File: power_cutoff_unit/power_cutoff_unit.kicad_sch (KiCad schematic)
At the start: 48 parts, among them J1 Conn_01x02, J10 Conn_01x04, J2 Conn_01x02, J3 Conn_01x02, J4 Conn_01x02, J5 Conn_01x02, J6 Conn_01x02, J7 Conn_01x02, J8 Conn_01x02, J9 Conn_01x02_Pin, K2 T9GS1L14-5, Q1 AO3400A, SW1 SW_DIP_x02, U1 ADuM120N, U2 STM32F303K8Tx, U3 ADP3338AKCZ-3.3, U4 MCP2562-E-SN, U6 LMZ14201H

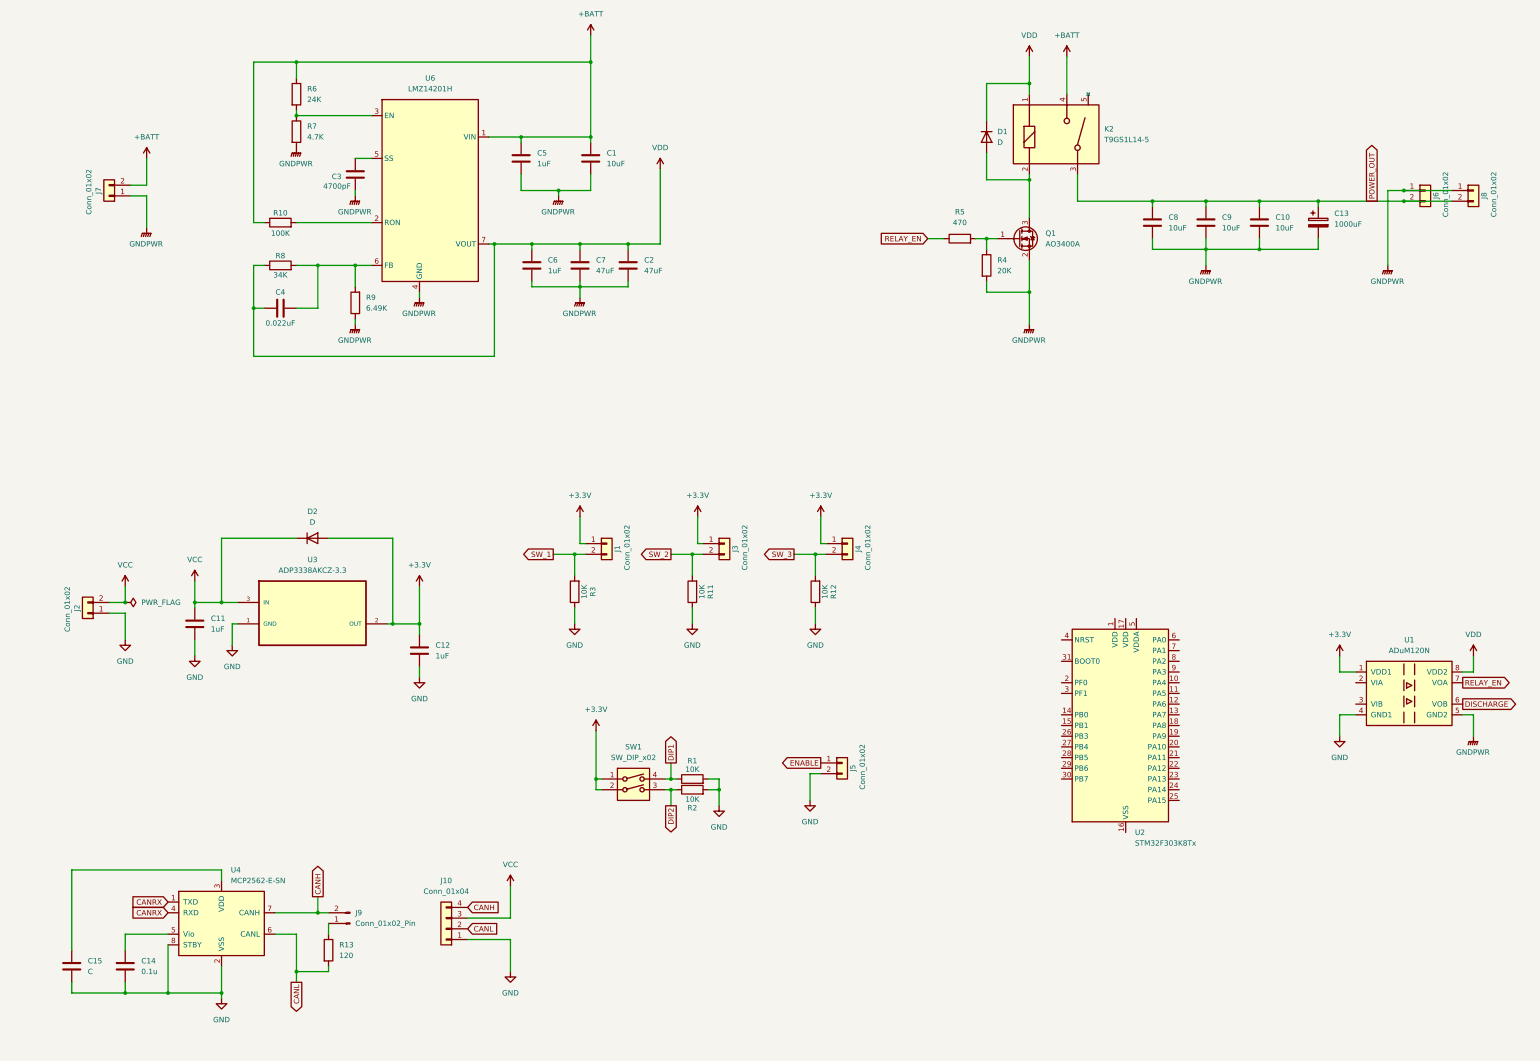
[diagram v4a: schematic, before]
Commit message: 5Vを選択的にした
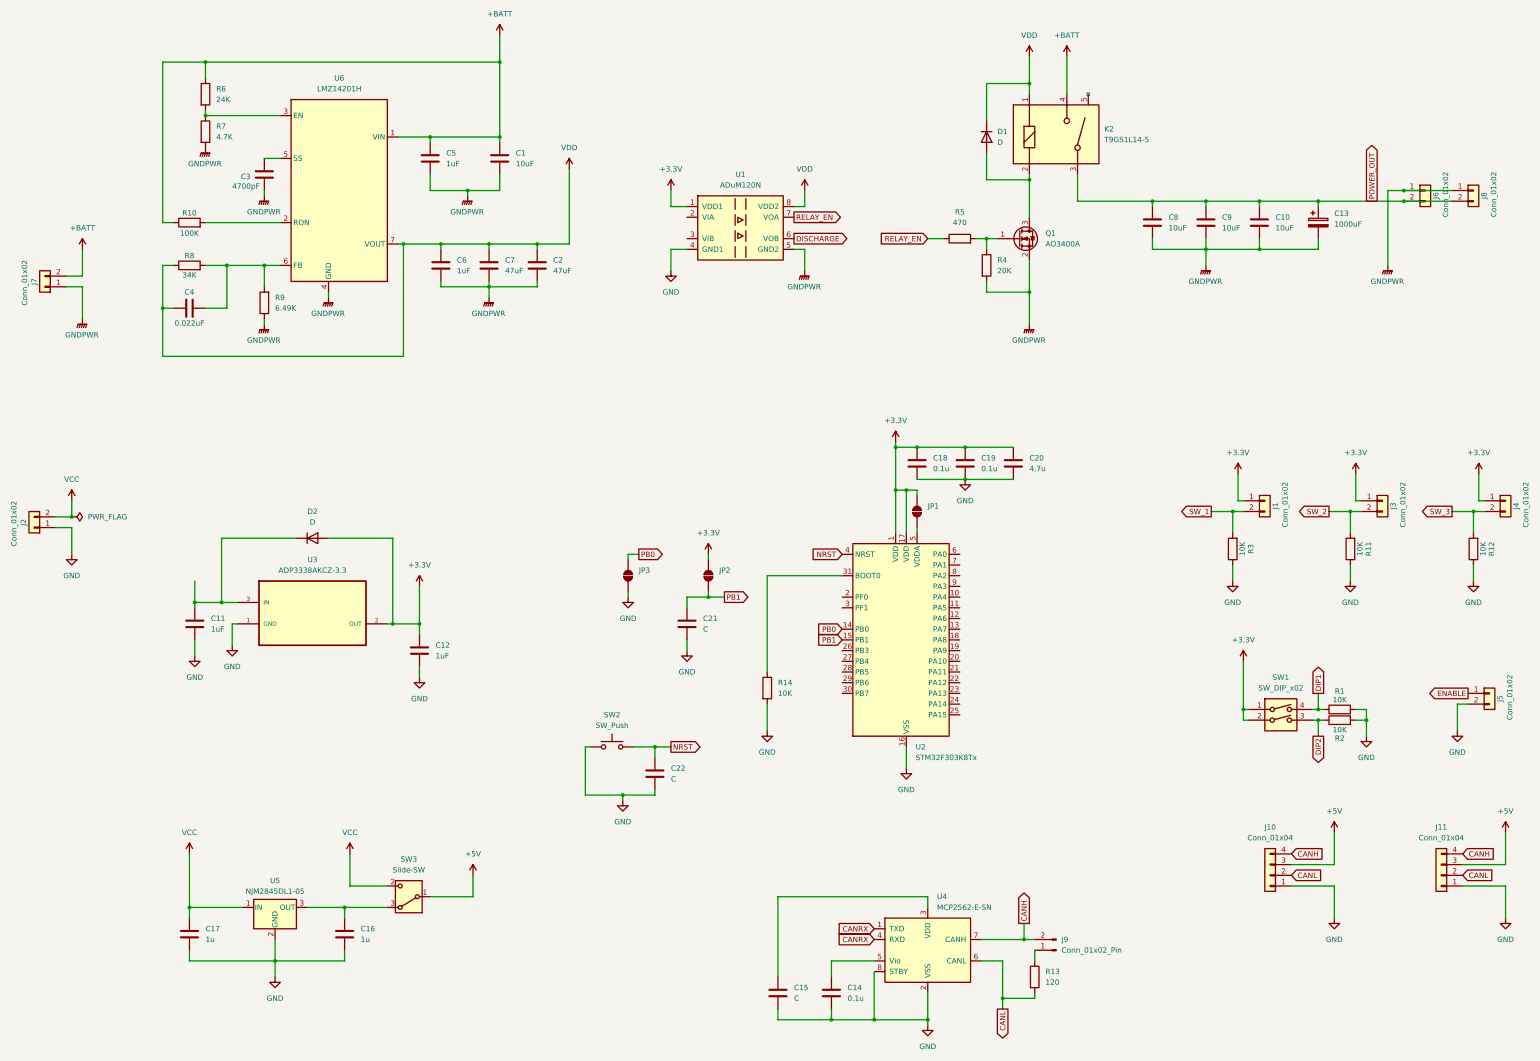
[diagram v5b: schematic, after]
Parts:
- added C16, C17: 1u, symbol Device:C
- added C18, C19: 0.1u, symbol Device:C
- added C20: 4.7u, symbol Device:C
- added C21, C22: C, symbol Device:C
- added J11: Conn_01x04, symbol Connector_Generic:Conn_01x04
- added JP1, JP2, JP3: SolderJumper_2_Open, symbol Jumper:SolderJumper_2_Open
- added R14: 10K, symbol Device:R
- added SW2: SW_Push, symbol Switch:SW_Push
- added SW3: Slide-SW, Button_Switch_THT:SW_Slide-03_Wuerth-WS-SLTV_10x2.5x6.4_P2.54mm, symbol Switch:SW_Wuerth_450301014042
- added U5: NJM2845DL1-05, Package_TO_SOT_SMD:TO-252-3_TabPin2, symbol Regulator_Linear:L7805
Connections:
- net +3.3V: now also U2.1 (VDD), U2.17 (VDD), C18.1, C19.1, C20.1, JP1.2 (B), JP2.2 (B)
- net CANH: now also J11.4 (Pin_4)
- net CANL: now also J11.2 (Pin_2)
- net GND: now also U2.16 (VSS), U2.32 (VSS), C16.2, C17.2, C18.2, C19.2, C20.2, C21.2, C22.2, J11.1 (Pin_1), JP3.1 (A), R14.2, SW2.1, U5.2 (GND)
- net VCC: now also C17.1, SW3.2 (C), U5.1 (IN); no longer C11.1, D2.1 (K), J10.3 (Pin_3), U3.3 (IN)
- net PB0: now reaches U2.14 (PB0)
- net PB0: now also JP3.2 (B)
- net PB1: now reaches U2.15 (PB1)
- net PB1: now also C21.1, JP2.1 (A)
- net at U2.31 (BOOT0): now also R14.1
- net NRST: now reaches U2.4 (NRST)
- net NRST: now also C22.1, SW2.2
- net at U2.5 (VDDA): now also JP1.1 (A)
- new net: C16.1, SW3.3 (A), U5.3 (OUT)
- new net: C11.1, D2.1 (K), U3.3 (IN)
- new net +5V: J10.3 (Pin_3), J11.3 (Pin_3), SW3.1 (B)
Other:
- moved on the sheet: C1, C14, C15, C2, C3, C4, C5, C6, C7, J1, J10, J2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

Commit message: CubeMXでプロジェクト作成
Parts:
- removed C8: 10uF, symbol Device:C
- added C23: 1000uF, Capacitor_THT:CP_Radial_D16.0mm_P7.50mm, symbol Device:C_Polarized
- added D3: LED, symbol Device:LED
- added Q2: SSM3K341R, Package_TO_SOT_SMD:SOT-23_Handsoldering, symbol Device:Q_NMOS_GDS
- added R15: 25, Package_TO_SOT_THT:TO-220-2_Vertical, symbol Device:R
- added R16, R18: 1K, symbol Device:R
- added R17: 20K, symbol Device:R
- C13: footprint (none) -> Capacitor_THT:CP_Radial_D16.0mm_P7.50mm
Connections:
- net +5V: now also C11.1, D2.1 (K), U3.3 (IN)
- net DISCHARGE: now also R18.1
- net GNDPWR: now also C23.2, Q2.3 (S), R17.2
- net POWER_OUT: now also C23.1, R15.1, R16.1
- new net: Q2.1 (G), R17.1, R18.2
- new net: D3.1 (K), Q2.2 (D), R15.2
- new net: D3.2 (A), R16.2
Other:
- company: (none) -> TMCIT-Arakawa
- title: (none) -> GN10PowerCutoffUnit
- moved on the sheet: C1, C10, C11, C12, C13, C14, C15, C16, C17, C18, C19, C2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

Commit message: MOSFET修正とCの値入れた。
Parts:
- removed Q1: AO3400A, Package_TO_SOT_SMD:SOT-23, symbol Transistor_FET:AO3400A
- removed Q2: SSM3K341R, Package_TO_SOT_SMD:SOT-23_Handsoldering, symbol Device:Q_NMOS_GDS
- added Q1, Q2: SSM3K341R, Package_TO_SOT_SMD:SOT-23_Handsoldering, symbol Device:Q_NMOS_GSD
- C13, C23: value 1000uF -> 1000u
- C15, C21, C22: value C -> 0.1u
- D1: value D -> SS2040FL; footprint (none) -> Diode_SMD:D_SOD-123F
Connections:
- net GNDPWR: now also Q1.2 (S), Q2.2 (S)
- net at D1.2 (A), K2.2: now also Q1.3 (D)
- net at R4.1, R5.2: now also Q1.1 (G)
- net at R17.1, R18.2: now also Q2.1 (G)
- net at D3.1 (K), R15.2: now also Q2.3 (D)
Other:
- moved on the sheet: D1
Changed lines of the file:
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@@
 	(wire
 		(pts
-			(xy 201.93 46.99) (xy 201.93 38.1)
+			(xy 194.31 46.99) (xy 194.31 38.1)
 		)
 		(stroke
@@
 	(wire
 		(pts
-			(xy 201.93 60.96) (xy 212.09 60.96)
+			(xy 194.31 60.96) (xy 212.09 60.96)
 		)
 		(stroke
@@
 	(wire
 		(pts
-			(xy 201.93 54.61) (xy 201.93 60.96)
+			(xy 194.31 54.61) (xy 194.31 60.96)
 		)
 		(stroke
@@
 	(wire
 		(pts
-			(xy 201.93 38.1) (xy 212.09 38.1)
+			(xy 194.31 38.1) (xy 212.09 38.1)
 		)
 		(stroke
@@
 	(symbol
 		(lib_id "Device:D")
-		(at 201.93 50.8 270)
+		(at 194.31 50.8 270)
 		(unit 1)
 		(exclude_from_sim no)
@@
 		(fields_autoplaced yes)
 		(property "Reference" "D1"
-			(at 204.47 49.5299 90)
+			(at 196.85 49.5299 90)
 			(effects
 				(font
@@
 			)
 		)
-		(property "Value" "D"
-			(at 204.47 52.0699 90)
+		(property "Value" "SS2040FL"
+			(at 196.85 52.0699 90)
 			(effects
 				(font
@@
 			)
 		)
-		(property "Footprint" ""
-			(at 201.93 50.8 0)
+		(property "Footprint" "Diode_SMD:D_SOD-123F"
+			(at 194.31 50.8 0)
 			(effects
 				(font
@@
 		)
 		(property "Datasheet" "~"
-			(at 201.93 50.8 0)
+			(at 194.31 50.8 0)
 			(effects
 				(font
@@
 		)
 		(property "Description" "Diode"
-			(at 201.93 50.8 0)
+			(at 194.31 50.8 0)
 			(effects
 				(font
@@
 		)
 		(property "Sim.Device" "D"
-			(at 201.93 50.8 0)
+			(at 194.31 50.8 0)
 			(effects
 				(font
@@
 		)
 		(property "Sim.Pins" "1=K 2=A"
-			(at 201.93 50.8 0)
+			(at 194.31 50.8 0)
 			(effects
 				(font
@@
 			)
 		)
-		(property "Value" "C"
+		(property "Value" "0.1u"
 			(at 142.24 264.1599 0)
 			(effects
@@
 	)
 	(symbol
-		(lib_id "Transistor_FET:AO3400A")
-		(at 209.55 74.93 0)
-		(unit 1)
-		(exclude_from_sim no)
-		(in_bom yes)
-		(on_board yes)
-		(dnp no)
-		(fields_autoplaced yes)
-		(property "Reference" "Q1"
-			(at 215.9 73.6599 0)
-			(effects
-				(font
-					(size 1.27 1.27)
-				)
-				(justify left)
-			)
-		)
-		(property "Value" "AO3400A"
-			(at 215.9 76.1999 0)
-			(effects
-				(font
-					(size 1.27 1.27)
-				)
-				(justify left)
-			)
-		)
-		(property "Footprint" "Package_TO_SOT_SMD:SOT-23"
-			(at 214.63 76.835 0)
-			(effects
-				(font
-					(size 1.27 1.27)
-					(italic yes)
-				)
-				(justify left)
-				(hide yes)
-			)
-		)
-		(property "Datasheet" "http://www.aosmd.com/pdfs/datasheet/AO3400A.pdf"
-			(at 214.63 78.74 0)
-			(effects
-				(font
-					(size 1.27 1.27)
-				)
-				(justify left)
-				(hide yes)
-			)
-		)
-		(property "Description" "30V Vds, 5.7A Id, N-Channel MOSFET, SOT-23"
-			(at 209.55 74.93 0)
-			(effects
-				(font
-					(size 1.27 1.27)
-				)
-				(hide yes)
-			)
-		)
-		(pin "3"
-		)
-		(pin "1"
-		)
-		(pin "2"
-		)
-		(instances
-			(project ""
-				(path "/a4c6539d-9123-466e-8ff2-1c6c45779bb9"
-					(reference "Q1")
-					(unit 1)
-				)
-			)
-		)
-	)
-	(symbol
 		(lib_id "power:GND")
 		(at 81.28 217.17 0)
@@
 			)
 		)
-		(property "Value" "C"
+		(property "Value" "0.1u"
 			(at 149.86 217.1699 0)
 			(effects
@@
 	)
 	(symbol
-		(lib_id "Device:Q_NMOS_GDS")
-		(at 354.33 68.58 0)
-		(unit 1)
-		(exclude_from_sim no)
-		(in_bom yes)
-		(on_board yes)
-		(dnp no)
-		(fields_autoplaced yes)
-		(property "Reference" "Q2"
-			(at 360.68 67.3099 0)
-			(effects
-				(font
-					(size 1.27 1.27)
-				)
-				(justify left)
-			)
-		)
-		(property "Value" "SSM3K341R"
-			(at 360.68 69.8499 0)
-			(effects
-				(font
-					(size 1.27 1.27)
-				)
-				(justify left)
-			)
-		)
-		(property "Footprint" "Package_TO_SOT_SMD:SOT-23_Handsoldering"
-			(at 359.41 66.04 0)
-			(effects
-				(font
-					(size 1.27 1.27)
-				)
-				(hide yes)
-			)
-		)
-		(property "Datasheet" "~"
-			(at 354.33 68.58 0)
-			(effects
-				(font
-					(size 1.27 1.27)
-				)
-				(hide yes)
-			)
-		)
-		(property "Description" "N-MOSFET transistor, gate/drain/source"
-			(at 354.33 68.58 0)
-			(effects
-				(font
-					(size 1.27 1.27)
-				)
-				(hide yes)
-			)
-		)
-		(pin "1"
-		)
-		(pin "2"
-		)
-		(pin "3"
-		)
-		(instances
-			(project ""
-				(path "/a4c6539d-9123-466e-8ff2-1c6c45779bb9"
-					(reference "Q2")
-					(unit 1)
-				)
-			)
-		)
-	)
-	(symbol
 		(lib_id "Device:C")
 		(at 231.14 68.58 0)
@@
 			)
 		)
-		(property "Value" "1000uF"
+		(property "Value" "1000u"
 			(at 261.62 68.9609 0)
 			(effects
@@
 			)
 		)
-		(property "Value" "C"
+		(property "Value" "0.1u"
 			(at 149.86 185.4199 0)
 			(effects
@@
 	)
 	(symbol
+		(lib_id "Device:Q_NMOS_GSD")
+		(at 209.55 74.93 0)
+		(unit 1)
+		(exclude_from_sim no)
+		(in_bom yes)
+		(on_board yes)
+		(dnp no)
+		(fields_autoplaced yes)
+		(property "Reference" "Q1"
+			(at 215.9 73.6599 0)
+			(effects
+				(font
+					(size 1.27 1.27)
+				)
+				(justify left)
+			)
+		)
+		(property "Value" "SSM3K341R"
+			(at 215.9 76.1999 0)
+			(effects
+				(font
+					(size 1.27 1.27)
+				)
+				(justify left)
+			)
+		)
+		(property "Footprint" "Package_TO_SOT_SMD:SOT-23_Handsoldering"
+			(at 214.63 72.39 0)
+			(effects
+				(font
+					(size 1.27 1.27)
+				)
+				(hide yes)
+			)
+		)
+		(property "Datasheet" "~"
+			(at 209.55 74.93 0)
+			(effects
+				(font
+					(size 1.27 1.27)
+				)
+				(hide yes)
+			)
+		)
+		(property "Description" "N-MOSFET transistor, gate/source/drain"
+			(at 209.55 74.93 0)
+			(effects
+				(font
+					(size 1.27 1.27)
+				)
+				(hide yes)
+			)
+		)
+		(pin "1"
+		)
+		(pin "3"
+		)
+		(pin "2"
+		)
+		(instances
+			(project "power_cutoff_unit"
+				(path "/a4c6539d-9123-466e-8ff2-1c6c45779bb9"
+					(reference "Q1")
+					(unit 1)
+				)
+			)
+		)
+	)
+	(symbol
 		(lib_id "Connector_Generic:Conn_01x02")
 		(at 327.66 182.88 0)
@@
 			)
 		)
-		(property "Value" "1000uF"
+		(property "Value" "1000u"
 			(at 275.59 68.9609 0)
 			(effects
@@
 					(unit 1)
 				)
+			)
+		)
+	)
+	(symbol
+		(lib_id "Device:Q_NMOS_GSD")
+		(at 354.33 68.58 0)
+		(unit 1)
+		(exclude_from_sim no)
+		(in_bom yes)
+		(on_board yes)
+		(dnp no)
+		(fields_autoplaced yes)
+		(property "Reference" "Q2"
+			(at 360.68 67.3099 0)
+			(effects
+				(font
+					(size 1.27 1.27)
+				)
+				(justify left)
+			)
+		)
+		(property "Value" "SSM3K341R"
+			(at 360.68 69.8499 0)
+			(effects
+				(font
+					(size 1.27 1.27)
+				)
+				(justify left)
+			)
+		)
+		(property "Footprint" "Package_TO_SOT_SMD:SOT-23_Handsoldering"
+			(at 359.41 66.04 0)
+			(effects
+				(font
+					(size 1.27 1.27)
+				)
+				(hide yes)
+			)
+		)
+		(property "Datasheet" "~"
+			(at 354.33 68.58 0)
+			(effects
+				(font
+					(size 1.27 1.27)
+				)
+				(hide yes)
+			)
+		)
+		(property "Description" "N-MOSFET transistor, gate/source/drain"
+			(at 354.33 68.58 0)
+			(effects
+				(font
+					(size 1.27 1.27)
+				)
+				(hide yes)
+			)
+		)
+		(pin "1"
+		)
+		(pin "3"
+		)
+		(pin "2"
+		)
+		(instances
+			(project ""
+				(path "/a4c6539d-9123-466e-8ff2-1c6c45779bb9"
+					(reference "Q2")
+					(unit 1)
+				)

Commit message: STM32のピン配置とインジケーターを追加
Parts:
- removed J5: Conn_01x02, Connector_JST:JST_XH_S2B-XH-A_1x02_P2.50mm_Horizontal, symbol Connector_Generic:Conn_01x02
- added BZ1: Buzzer, Buzzer_Beeper:Buzzer_12x9.5RM7.6, symbol Device:Buzzer
- added C8: 1u, symbol Device:C
- added D10, D11, D12, D17, D18, D19, D20, D4, D5, D6, D7, D8, D9: LED, symbol Device:LED
- added J5: Conn_01x03, symbol Connector_Generic:Conn_01x03
- added Q3: BSS138, Package_TO_SOT_SMD:SOT-23, symbol Transistor_FET:AO3400A
- added R19, R21, R22, R23, R24, R25, R26, R27, R34: 1K, symbol Device:R
- added R20: 4.7K, symbol Device:R
- added R32: 470, Resistor_SMD:R_0603_1608Metric, symbol Device:R
- added R33: 20K, Resistor_SMD:R_0603_1608Metric, symbol Device:R
- R11, R12, R3: value 10K -> 1K
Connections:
- net +3.3V: now also BZ1.1 (+), C8.1, J5.3 (Pin_3), R21.1
- net +5V: now also R23.1
- net +BATT: now also R20.1
- net DIP1: now also U2.26 (PB3)
- net DIP2: now also U2.27 (PB4)
- net DISCHARGE: now also U1.3 (VIB), U2.7 (PA1); no longer R18.1, U1.6 (VOB)
- net ENABLE: now also U2.18 (PA8), J5.2 (Pin_2)
- net GND: now also C8.2, D10.1 (K), D20.1 (K), D4.1 (K), D5.1 (K), D6.1 (K), D7.1 (K), D8.1 (K), D9.1 (K), J5.1 (Pin_1), Q3.2 (S), R33.2
- net GNDPWR: now also D11.1 (K), D12.1 (K)
- net RELAY_EN: now also U1.2 (VIA), U2.8 (PA2); no longer R5.1, U1.7 (VOA)
- net SW_1: now also U2.28 (PB5), D17.2 (A); no longer R3.2
- net SW_2: now also U2.29 (PB6), D18.2 (A); no longer R11.2
- net SW_3: now also U2.30 (PB7), D19.2 (A); no longer R12.2
- net VCC: now also R22.1; no longer SW3.2 (C)
- net VDD: now also R19.1
- net CONNECTION_2: now reaches U2.10 (PA4)
- net CONNECTION_2: now also R25.1
- net CONNECTION_3: now reaches U2.11 (PA5)
- net CONNECTION_3: now also R26.1
- net CONNECTION_4: now reaches U2.12 (PA6)
- net CONNECTION_4: now also R27.1
- net UART1_TX: now reaches U2.19 (PA9)
- net UART1_RX: now reaches U2.20 (PA10)
- net CAN_RX: now reaches U2.21 (PA11)
- net CAN_TX: now reaches U2.22 (PA12)
- net SWDIO: now reaches U2.23 (PA13)
- net SWCLK: now reaches U2.24 (PA14)
- net BUZZER: now reaches U2.25 (PA15)
- net BUZZER: now also R32.1
- net CONNECTION_1: now reaches U2.9 (PA3)
- net CONNECTION_1: now also R24.1
- net POWER_OUT: no longer names the net of C10.1, C13.1, C23.1, C9.1, J6.2 (Pin_2), J8.2 (Pin_2), K2.3, R15.1, R16.1
- new net: D4.2 (A), R27.2
- new net: D7.2 (A), R24.2
- new net: D11.2 (A), R20.2
- new net: D6.2 (A), R25.2
- new net: BZ1.2 (-), Q3.3 (D)
- new net: D10.2 (A), R23.2
- new net: D19.1 (K), R12.2
- new net: D5.2 (A), R26.2
- new net: Q3.1 (G), R32.2, R33.1
- new net: D17.1 (K), R3.2
- new net: D18.1 (K), R11.2
- new net: D12.2 (A), R19.2
- new net: D9.2 (A), R22.2
- new net: D20.2 (A), R34.2
- new net: D8.2 (A), R21.2
- new net DEBUG: R34.1
- new net isolated_DISCHARGE: R18.1, U1.6 (VOB)
- new net isolated_RELAY_EN: R5.1, U1.7 (VOA)
- no-connect marks 0 -> 5
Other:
- moved on the sheet: D3, J1, J2, J3, J4, Q2, R1, R11, R12, R15, R16, R17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
